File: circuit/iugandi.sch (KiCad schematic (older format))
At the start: 1 part

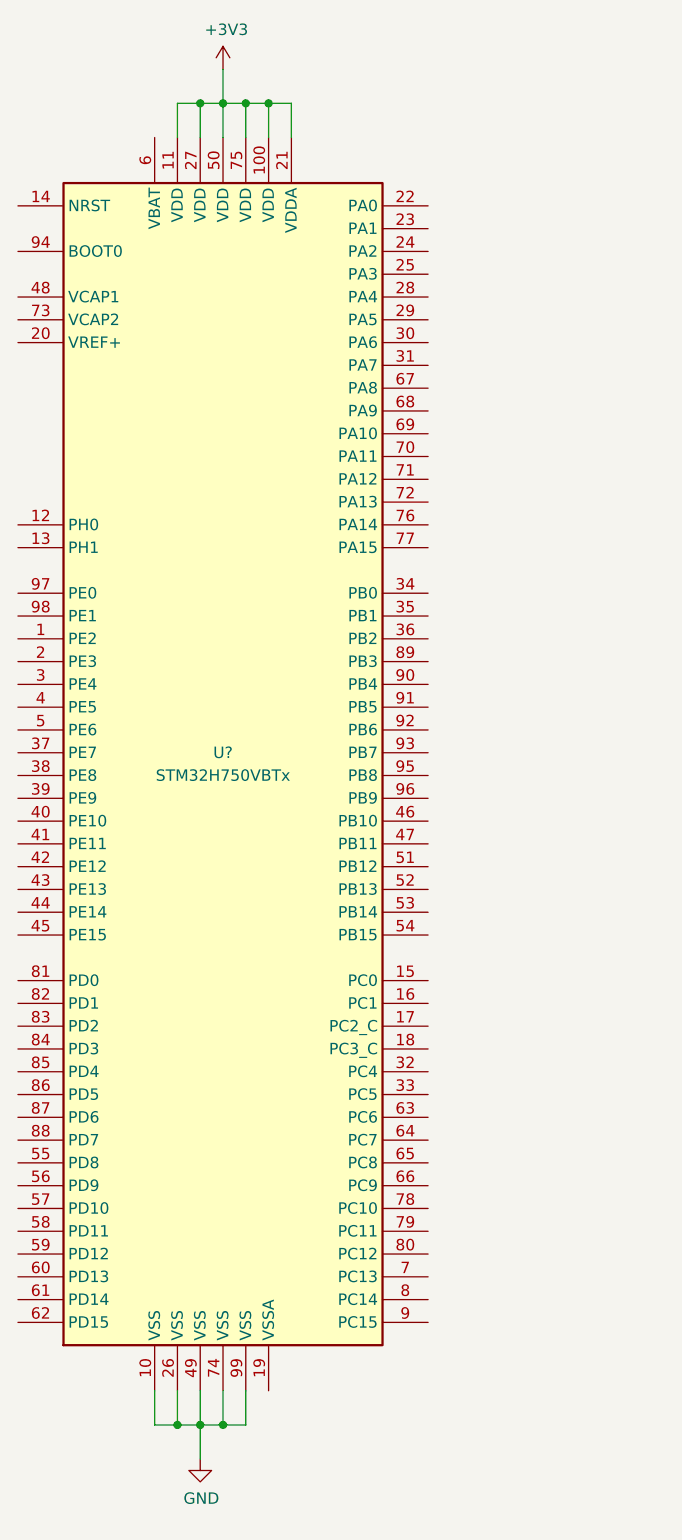
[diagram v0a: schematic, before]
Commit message: Edited the schematic and removed unused files
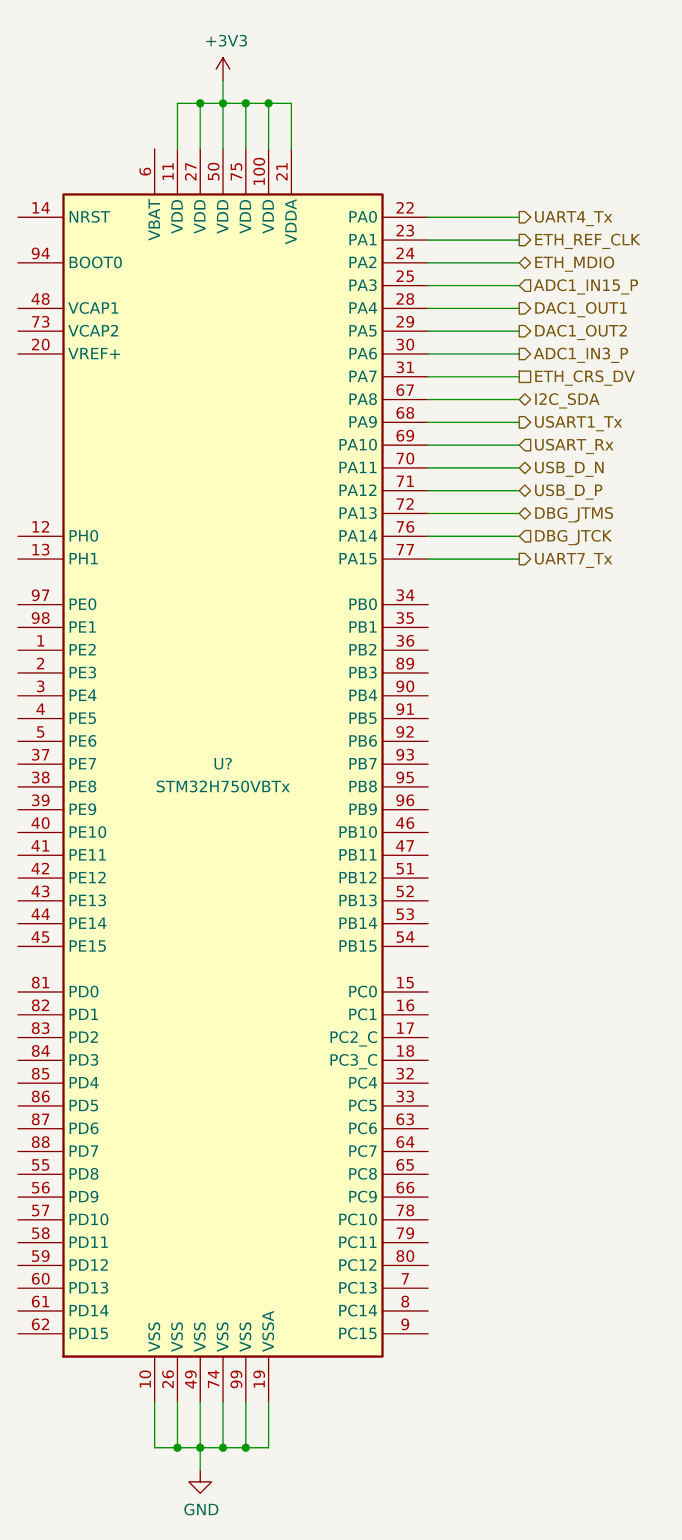
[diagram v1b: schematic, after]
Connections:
- net GND: now also U?.19 (VSSA)
- net UART4_Tx: now reaches U?.22 (PA0)
- net ETH_REF_CLK: now reaches U?.23 (PA1)
- net ETH_MDIO: now reaches U?.24 (PA2)
- net ADC1_IN15_P: now reaches U?.25 (PA3)
- net DAC1_OUT1: now reaches U?.28 (PA4)
- net DAC1_OUT2: now reaches U?.29 (PA5)
- net ADC1_IN3_P: now reaches U?.30 (PA6)
- net ETH_CRS_DV: now reaches U?.31 (PA7)
- net I2C_SDA: now reaches U?.67 (PA8)
- net USART1_Tx: now reaches U?.68 (PA9)
- net USART_Rx: now reaches U?.69 (PA10)
- net USB_D_N: now reaches U?.70 (PA11)
- net USB_D_P: now reaches U?.71 (PA12)
- net DBG_JTMS: now reaches U?.72 (PA13)
- net DBG_JTCK: now reaches U?.76 (PA14)
- net UART7_Tx: now reaches U?.77 (PA15)
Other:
- moved on the sheet: U?
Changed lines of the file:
@@
 $EndDescr
+$Comp
+L power:+3V3 #PWR?
+U 1 1 61A0C504
+P 4000 900
+F 0 "#PWR?" H 4000 750 50  0001 C CNN
+F 1 "+3V3" H 4015 1073 50  0000 C CNN
+F 2 "" H 4000 900 50  0001 C CNN
+F 3 "" H 4000 900 50  0001 C CNN
+	1    4000 900
+	1    0    0    -1
+$EndComp
+$Comp
+L power:GND #PWR?
+U 1 1 61A0F694
+P 3900 7000
+F 0 "#PWR?" H 3900 6750 50  0001 C CNN
+F 1 "GND" H 3905 6827 50  0000 C CNN
+F 2 "" H 3900 7000 50  0001 C CNN
+F 3 "" H 3900 7000 50  0001 C CNN
+	1    3900 7000
+	1    0    0    -1
+$EndComp
 $Comp
 L Microcontroller:STM32H750VBTx U?
 U 1 1 61A087E3
-P 4000 3850
-F 0 "U?" H 4000 3850 50  0000 C CNN
-F 1 "STM32H750VBTx" H 4000 3750 50  0000 C CNN
-F 2 "Package_QFP:LQFP-100_14x14mm_P0.5mm" H 3300 1250 50  0001 R CNN
-F 3 "https://www.st.com/resource/en/datasheet/stm32h750ib.pdf" H 4000 3850 50  0001 C CNN
-	1    4000 3850
+P 4000 3900
+F 0 "U?" H 4000 3900 50  0000 C CNN
+F 1 "STM32H750VBTx" H 4000 3800 50  0000 C CNN
+F 2 "Package_QFP:LQFP-100_14x14mm_P0.5mm" H 3300 1300 50  0001 R CNN
+F 3 "https://www.st.com/resource/en/datasheet/stm32h750ib.pdf" H 4000 3900 50  0001 C CNN
+	1    4000 3900
 	1    0    0    -1
 $EndComp
-$Comp
-L power:+3V3 #PWR?
-U 1 1 61A0C504
-P 4000 850
-F 0 "#PWR?" H 4000 700 50  0001 C CNN
-F 1 "+3V3" H 4015 1023 50  0000 C CNN
-F 2 "" H 4000 850 50  0001 C CNN
-F 3 "" H 4000 850 50  0001 C CNN
-	1    4000 850
-	1    0    0    -1
-$EndComp
+Text HLabel 5300 1500 2    50   Output ~ 0
+UART4_Tx
+Text HLabel 5300 1600 2    50   Output ~ 0
+ETH_REF_CLK
+Text HLabel 5300 1700 2    50   BiDi ~ 0
+ETH_MDIO
+Text HLabel 5300 1800 2    50   Input ~ 0
+ADC1_IN15_P
+Text HLabel 5300 1900 2    50   Output ~ 0
+DAC1_OUT1
+Text HLabel 5300 2000 2    50   Output ~ 0
+DAC1_OUT2
+Text HLabel 5300 2100 2    50   Output ~ 0
+ADC1_IN3_P
+Text HLabel 5300 2200 2    50   UnSpc ~ 0
+ETH_CRS_DV
+Text HLabel 5300 2300 2    50   BiDi ~ 0
+I2C_SDA
+Text HLabel 5300 2400 2    50   Output ~ 0
+USART1_Tx
+Text HLabel 5300 2500 2    50   Input ~ 0
+USART_Rx
+Text HLabel 5300 2600 2    50   BiDi ~ 0
+USB_D_N
+Text HLabel 5300 2700 2    50   BiDi ~ 0
+USB_D_P
 Wire Wire Line
-	3800 1150 3800 1000
+	4900 1500 5300 1500
+Wire Wire Line
+	5300 1600 4900 1600
+Wire Wire Line
+	4900 1700 5300 1700
+Wire Wire Line
+	5300 1800 4900 1800
+Wire Wire Line
+	4900 1900 5300 1900
+Wire Wire Line
+	5300 2000 4900 2000
+Wire Wire Line
+	4900 2100 5300 2100
+Wire Wire Line
+	5300 2200 4900 2200
+Wire Wire Line
+	4900 2300 5300 2300
+Wire Wire Line
+	5300 2400 4900 2400
+Wire Wire Line
+	4900 2500 5300 2500
+Wire Wire Line
+	5300 2600 4900 2600
+Wire Wire Line
+	4900 2700 5300 2700
+Text HLabel 5300 2800 2    50   BiDi ~ 0
+DBG_JTMS
+Text HLabel 5300 2900 2    50   Input ~ 0
+DBG_JTCK
+Text HLabel 5300 3000 2    50   Output ~ 0
+UART7_Tx
+Wire Wire Line
+	5300 3000 4900 3000
+Wire Wire Line
+	4900 2900 5300 2900
+Wire Wire Line
+	5300 2800 4900 2800
+Wire Wire Line
+	3800 1200 3800 1000
 Wire Wire Line
 	3800 1000 3900 1000
 Wire Wire Line
-	4200 1000 4200 1150
+	4300 1000 4300 1200
 Wire Wire Line
-	4000 850  4000 1000
+	3900 1200 3900 1000
+Connection ~ 3900 1000
+Wire Wire Line
+	3900 1000 4000 1000
+Wire Wire Line
+	4000 1000 4000 1200
 Connection ~ 4000 1000
 Wire Wire Line
 	4000 1000 4100 1000
 Wire Wire Line
-	3900 1150 3900 1000
-Connection ~ 3900 1000
-Wire Wire Line
-	3900 1000 4000 1000
-Wire Wire Line
-	4000 1150 4000 1000
-Wire Wire Line
-	4100 1150 4100 1000
+	4100 1200 4100 1000
 Connection ~ 4100 1000
 Wire Wire Line
 	4100 1000 4200 1000
-$Comp
-L power:GND #PWR?
-U 1 1 61A0F694
-P 3900 6950
-F 0 "#PWR?" H 3900 6700 50  0001 C CNN
-F 1 "GND" H 3905 6777 50  0000 C CNN
-F 2 "" H 3900 6950 50  0001 C CNN
-F 3 "" H 3900 6950 50  0001 C CNN
-	1    3900 6950
-	1    0    0    -1
-$EndComp
 Wire Wire Line
-	3700 6650 3700 6800
+	4200 1000 4200 1200
+Connection ~ 4200 1000
 Wire Wire Line
-	3700 6800 3800 6800
+	4200 1000 4300 1000
 Wire Wire Line
-	4100 6800 4100 6650
+	4000 1000 4000 900
 Wire Wire Line
-	3900 6950 3900 6800
-Connection ~ 3900 6800
+	3700 6700 3700 6900
 Wire Wire Line
-	3800 6650 3800 6800
-Connection ~ 3800 6800
+	3700 6900 3800 6900
 Wire Wire Line
-	3800 6800 3900 6800
+	4200 6900 4200 6700
 Wire Wire Line
-	3900 6650 3900 6800
+	4100 6700 4100 6900
+Connection ~ 4100 6900
 Wire Wire Line
-	4000 6650 4000 6800
+	4100 6900 4200 6900
 Wire Wire Line
-	3900 6800 4000 6800
+	4000 6900 4000 6700
+Connection ~ 4000 6900
 Wire Wire Line
-	4000 6800 4100 6800
-Connection ~ 4000 6800
+	4000 6900 4100 6900
 Wire Wire Line
-	4300 1150 4300 1000
+	3900 6700 3900 6900
+Connection ~ 3900 6900
 Wire Wire Line
-	4300 1000 4200 1000
-Connection ~ 4200 1000
+	3900 6900 4000 6900
+Wire Wire Line
+	3800 6900 3800 6700
+Connection ~ 3800 6900
+Wire Wire Line
+	3800 6900 3900 6900
+Wire Wire Line
+	3900 6900 3900 7000
 $EndSCHEMATC
